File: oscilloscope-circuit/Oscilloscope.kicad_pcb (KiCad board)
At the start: 4 copper layers, 63.5 x 63.5 mm, 84 parts, among them J1 Ch1 BNC, J2 PMOD B, J3 PMOD C, J4 SPI header, J5 1 KHz ±3.0V, J6 GND, J7 3.0VDC, J8 -3.0VDC, U1 LTC2267-14, U2 TLV75718PDBV, U3 MIC5501-3.0YM5, U4 LM2776, U5 TC59, U6 GDT CG775, U7 ADA4817-1, U8 LT6411, U9 TLV2371DBV

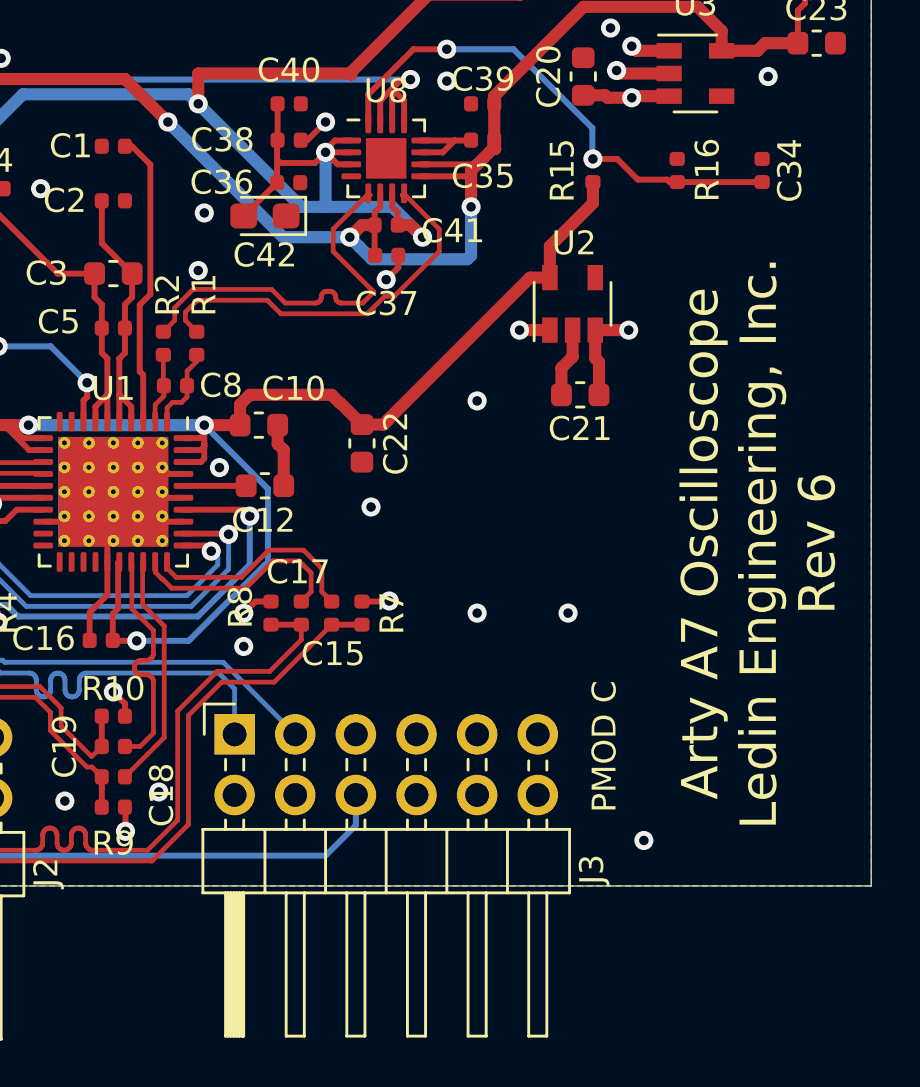
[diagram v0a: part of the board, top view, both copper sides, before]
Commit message: Add oscilloscope circuit schematics and reorganize docs
Added KiCad schematic files for the oscilloscope circuit, including ADC, analog inputs, calibration, PMOD ports, power supply, and SPI. Moved project documentation files to the docs/ directory. Updated README.md to improve clarity.
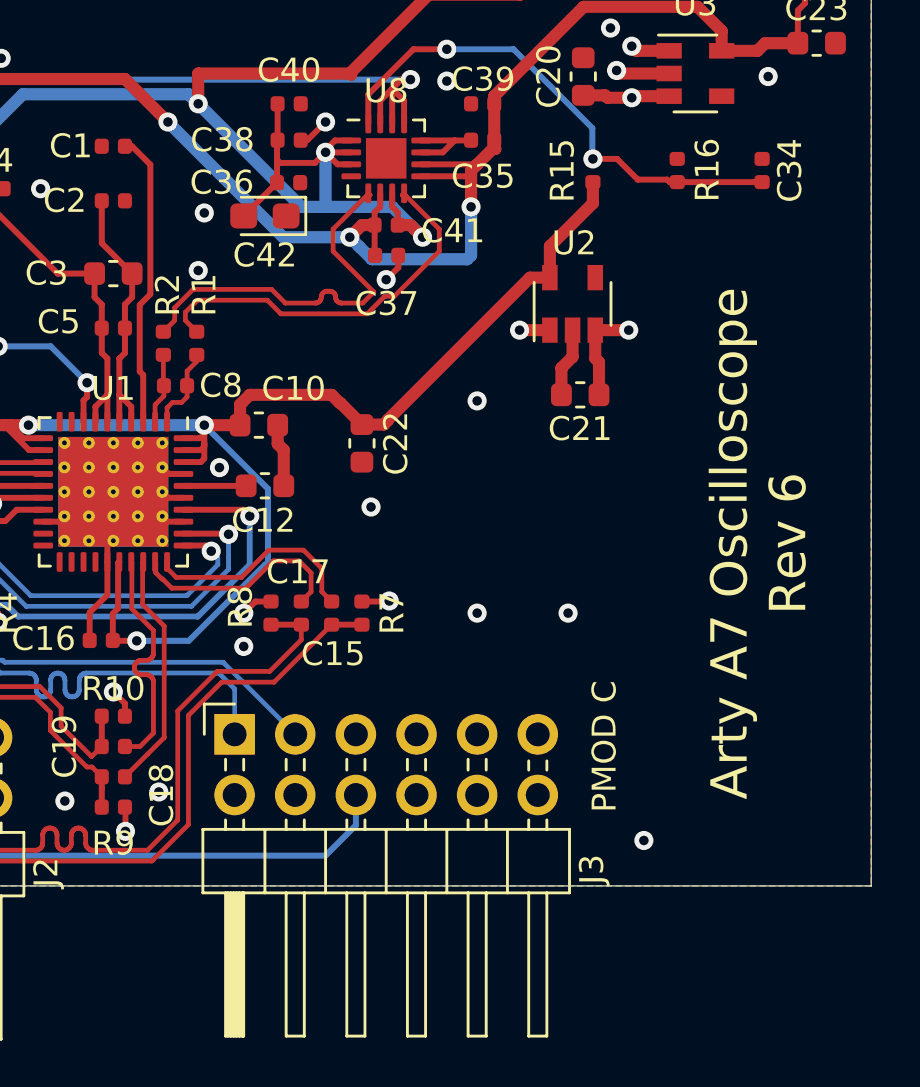
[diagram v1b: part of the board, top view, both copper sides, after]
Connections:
- net ~CS renamed ~{CS}
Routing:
- added copper zone on In2.Cu, net +3V3
- added copper zone on In1.Cu, net GND
- removed copper zone on +3V3, net +3V3
- removed copper zone on GND, net GND
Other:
- net class Default removed
- net class Power removed
- board text added: "Arty A7 Oscilloscope Rev 6"
- board text removed: "Arty A7 Oscilloscope Ledin Engineering, Inc. Rev 6"
